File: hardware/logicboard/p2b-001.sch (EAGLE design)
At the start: 54 parts, among them IC1 74LS06N, IC2 4066N, J1 MKR, J2 GPIO, J3 Vcc, J4 RLY, J5 SPI, J7 DIN5, J8 DIN5, J9 DIN5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

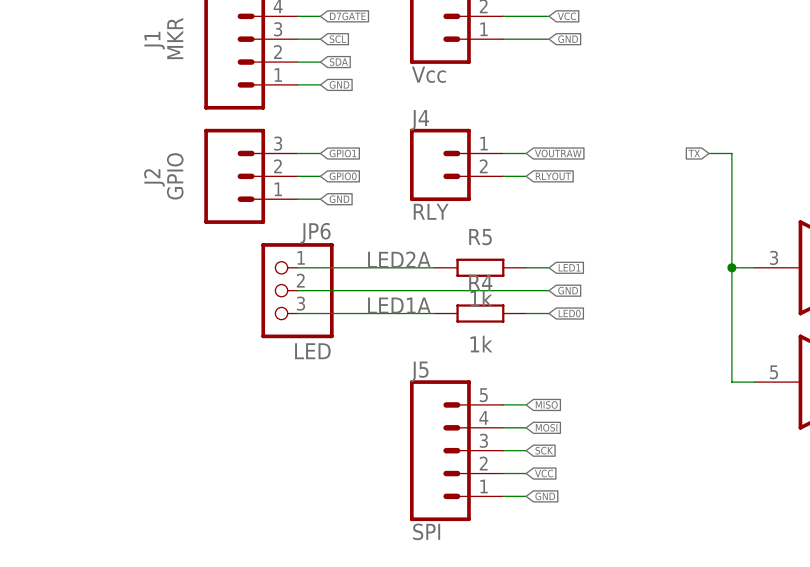
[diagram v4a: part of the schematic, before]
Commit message: Added silk of LED0/1.
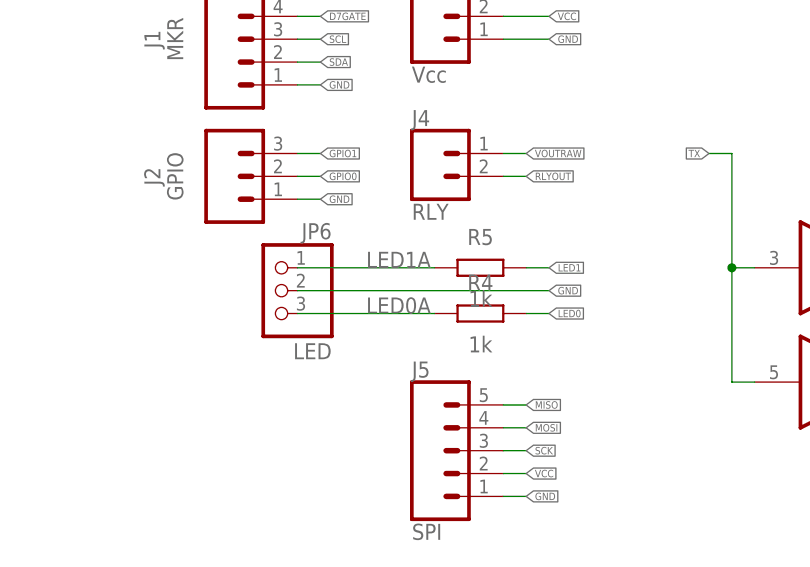
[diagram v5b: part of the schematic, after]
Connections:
- removed net LED2A: JP6.1, R5.1
- new net LED0A: JP6.3, R4.1
- net LED1A: now also JP6.1, R5.1; no longer JP6.3, R4.1
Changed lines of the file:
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@@
 </segment>
 </net>
-<net name="LED2A" class="0">
+<net name="LED1A" class="0">
 <segment>
 <wire x1="88.9" y1="38.1" x2="73.66" y2="38.1" width="0.1524" layer="91"/>
@@
 </segment>
 </net>
-<net name="LED1A" class="0">
+<net name="LED0A" class="0">
 <segment>
 <wire x1="88.9" y1="33.02" x2="73.66" y2="33.02" width="0.1524" layer="91"/>

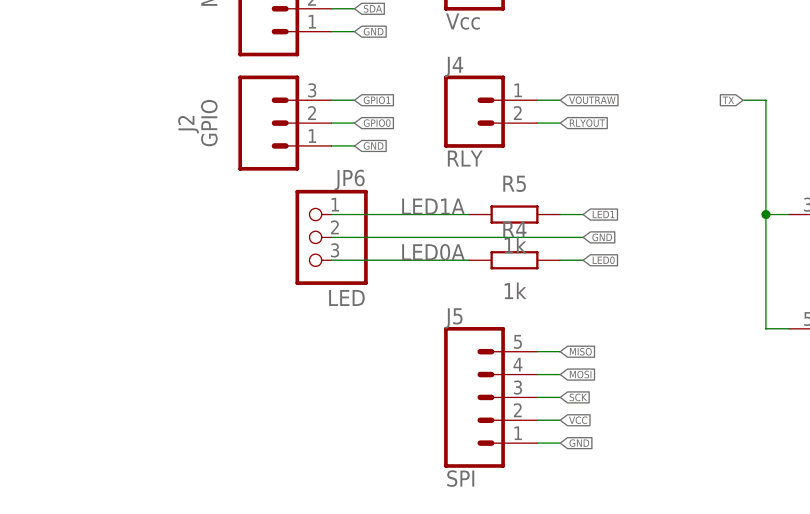
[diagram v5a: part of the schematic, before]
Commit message: Added J6 (LED connector).
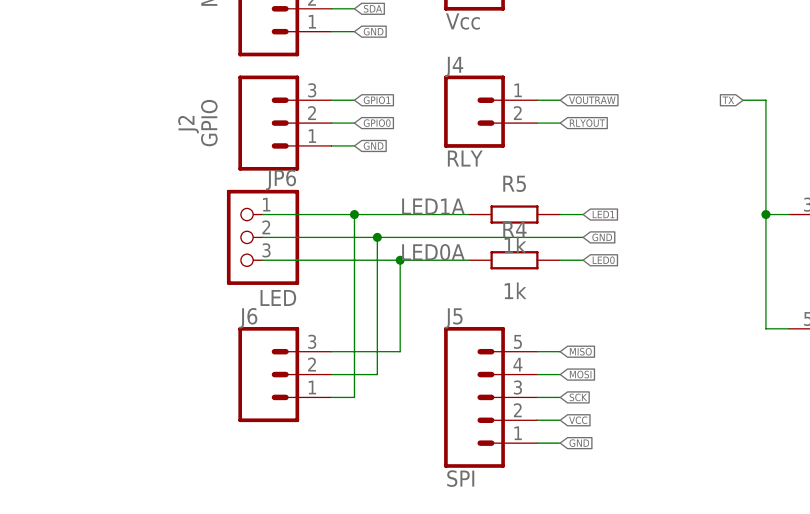
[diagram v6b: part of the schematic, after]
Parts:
- added J6: (no value), SparkFun-Connectors:CONN_03JST-PTH-VERT
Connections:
- net GND: now also J6.2
- net LED0A: now also J6.3
- net LED1A: now also J6.1
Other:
- moved on the sheet: JP6
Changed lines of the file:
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@@
 <part name="P+5" library="supply1" library_urn="urn:adsk.eagle:library:371" deviceset="VCC" device=""/>
 <part name="SV3" library="con-ml" library_urn="urn:adsk.eagle:library:164" deviceset="ML14E" device="" package3d_urn="urn:adsk.eagle:package:8693/1"/>
+<part name="J6" library="SparkFun-Connectors" library_urn="urn:adsk.eagle:library:513" deviceset="CONN_03" device="JST-PTH-VERT" package3d_urn="urn:adsk.eagle:package:38080/1"/>
 </parts>
 <sheets>
@@
 <attribute name="VALUE" x="93.98" y="35.56" size="1.778" layer="96" align="top-center"/>
 </instance>
-<instance part="JP6" gate="A" x="71.12" y="35.56" smashed="yes" rot="MR0">
-<attribute name="NAME" x="77.47" y="41.275" size="1.778" layer="95" rot="MR0"/>
-<attribute name="VALUE" x="77.47" y="27.94" size="1.778" layer="96" rot="MR0"/>
+<instance part="JP6" gate="A" x="63.5" y="35.56" smashed="yes" rot="MR0">
+<attribute name="NAME" x="69.85" y="41.275" size="1.778" layer="95" rot="MR0"/>
+<attribute name="VALUE" x="69.85" y="27.94" size="1.778" layer="96" rot="MR0"/>
 </instance>
 <instance part="JP5" gate="A" x="30.48" y="233.68" smashed="yes" rot="R180">
@@
 <attribute name="NAME" x="337.82" y="215.138" size="1.778" layer="95"/>
 <attribute name="VALUE" x="335.026" y="212.979" size="1.778" layer="96"/>
+</instance>
+<instance part="J6" gate="J$1" x="66.04" y="20.32" smashed="yes">
+<attribute name="VALUE" x="63.5" y="12.954" size="1.778" layer="96" font="vector"/>
+<attribute name="NAME" x="63.5" y="25.908" size="1.778" layer="95" font="vector"/>
 </instance>
 </instances>
@@
 <segment>
 <label x="101.6" y="35.56" size="0.8128" layer="95" xref="yes"/>
-<wire x1="73.66" y1="35.56" x2="101.6" y2="35.56" width="0.1524" layer="91"/>
+<wire x1="66.04" y1="35.56" x2="78.74" y2="35.56" width="0.1524" layer="91"/>
 <pinref part="JP6" gate="A" pin="2"/>
+<pinref part="J6" gate="J$1" pin="2"/>
+<wire x1="78.74" y1="35.56" x2="101.6" y2="35.56" width="0.1524" layer="91"/>
+<wire x1="73.66" y1="20.32" x2="78.74" y2="20.32" width="0.1524" layer="91"/>
+<wire x1="78.74" y1="20.32" x2="78.74" y2="35.56" width="0.1524" layer="91"/>
+<junction x="78.74" y="35.56"/>
 </segment>
 <segment>
@@
 <net name="LED1A" class="0">
 <segment>
-<wire x1="88.9" y1="38.1" x2="73.66" y2="38.1" width="0.1524" layer="91"/>
+<wire x1="88.9" y1="38.1" x2="76.2" y2="38.1" width="0.1524" layer="91"/>
 <label x="81.28" y="38.1" size="1.778" layer="95"/>
 <pinref part="R5" gate="G$1" pin="1"/>
 <pinref part="JP6" gate="A" pin="1"/>
+<pinref part="J6" gate="J$1" pin="1"/>
+<wire x1="76.2" y1="38.1" x2="66.04" y2="38.1" width="0.1524" layer="91"/>
+<wire x1="73.66" y1="17.78" x2="76.2" y2="17.78" width="0.1524" layer="91"/>
+<wire x1="76.2" y1="17.78" x2="76.2" y2="38.1" width="0.1524" layer="91"/>
+<junction x="76.2" y="38.1"/>
 </segment>
 </net>
@@
 <net name="LED0A" class="0">
 <segment>
-<wire x1="88.9" y1="33.02" x2="73.66" y2="33.02" width="0.1524" layer="91"/>
+<wire x1="88.9" y1="33.02" x2="81.28" y2="33.02" width="0.1524" layer="91"/>
 <label x="81.28" y="33.02" size="1.778" layer="95"/>
 <pinref part="R4" gate="G$1" pin="1"/>
 <pinref part="JP6" gate="A" pin="3"/>
-</segment>
-</net>
+<pinref part="J6" gate="J$1" pin="3"/>
+<wire x1="81.28" y1="33.02" x2="66.04" y2="33.02" width="0.1524" layer="91"/>
+<wire x1="73.66" y1="22.86" x2="81.28" y2="22.86" width="0.1524" layer="91"/>
+<wire x1="81.28" y1="22.86" x2="81.28" y2="33.02" width="0.1524" layer="91"/>
+<junction x="81.28" y="33.02"/>
+</segment>
+</net>

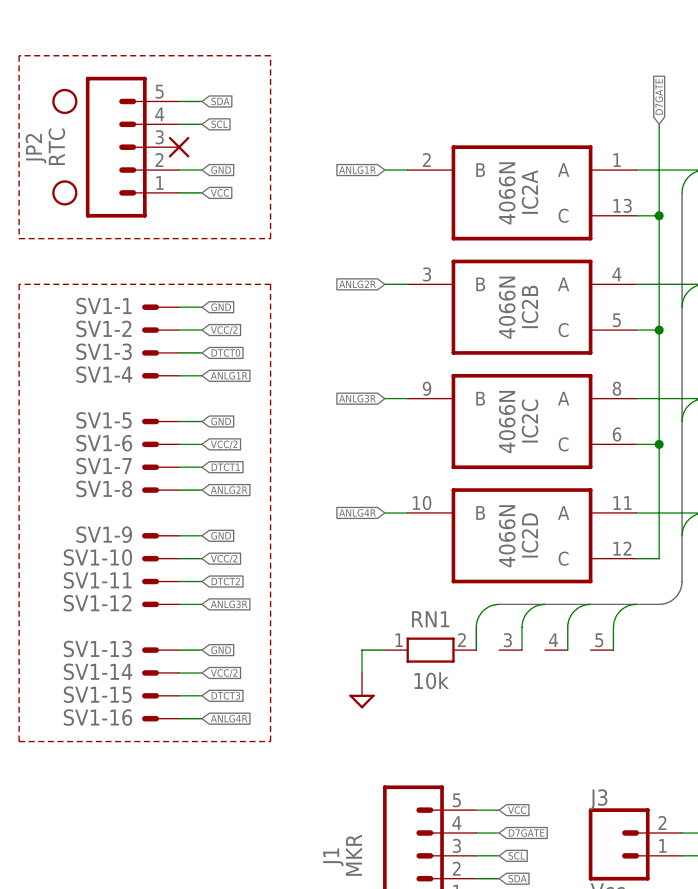
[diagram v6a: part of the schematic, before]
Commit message: Re-arranged GeekPort 2.0.
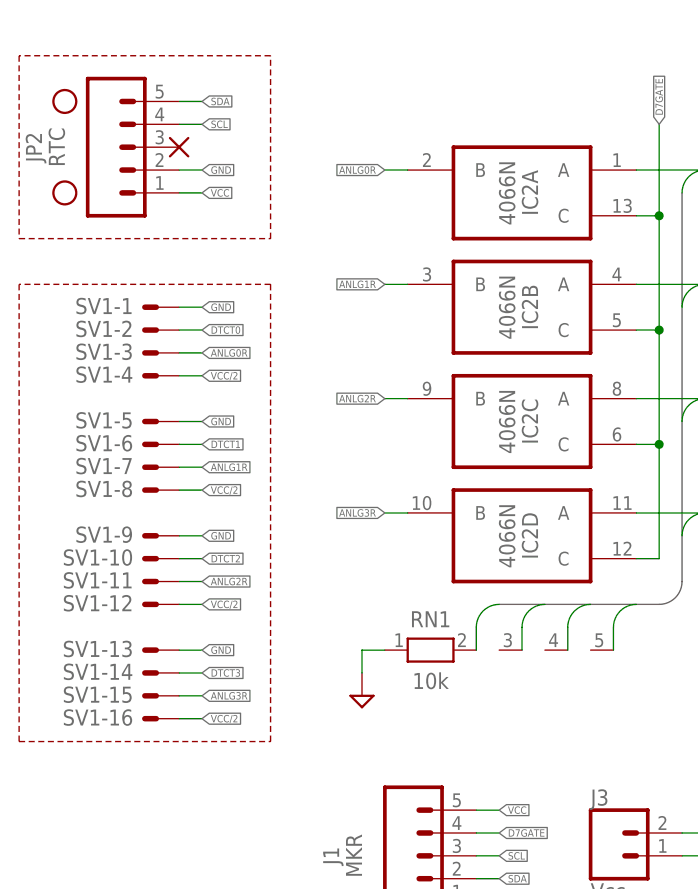
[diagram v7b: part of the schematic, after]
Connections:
- removed net ANLG4R: IC2D.B, SV1-16.S
- new net ANLG0R: IC2A.B, SV1-3.S
- net ANLG1R: now also IC2B.B, SV1-7.S; no longer IC2A.B, SV1-4.S
- net ANLG2R: now also IC2C.B, SV1-11.S; no longer IC2B.B, SV1-8.S
- net ANLG3R: now also IC2D.B, SV1-15.S; no longer IC2C.B, SV1-12.S
- net DTCT0: now also SV1-2.S; no longer SV1-3.S
- net DTCT1: now also SV1-6.S; no longer SV1-7.S
- net DTCT2: now also SV1-10.S; no longer SV1-11.S
- net DTCT3: now also SV1-14.S; no longer SV1-15.S
- net VCC/2: now also SV1-12.S, SV1-16.S, SV1-4.S, SV1-8.S; no longer SV1-10.S, SV1-14.S, SV1-2.S, SV1-6.S
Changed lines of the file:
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@@
-</segment>
-<segment>
-<pinref part="SV1" gate="-3" pin="S"/>
-<wire x1="40.64" y1="119.38" x2="43.18" y2="119.38" width="0.1524" layer="91"/>
-<label x="43.18" y="119.38" size="0.8128" layer="95" xref="yes"/>
 </segment>
 <segment>
@@
 <label x="330.2" y="231.14" size="0.8128" layer="95" rot="R90" xref="yes"/>
 </segment>
+<segment>
+<wire x1="40.64" y1="121.92" x2="43.18" y2="121.92" width="0.1524" layer="91"/>
+<pinref part="SV1" gate="-2" pin="S"/>
+<label x="43.18" y="121.92" size="0.8128" layer="95" xref="yes"/>
+</segment>
 </net>
 <net name="DTCT1" class="0">
@@
 </segment>
 <segment>
-<pinref part="SV1" gate="-7" pin="S"/>
-<wire x1="40.64" y1="106.68" x2="43.18" y2="106.68" width="0.1524" layer="91"/>
-<label x="43.18" y="106.68" size="0.8128" layer="95" xref="yes"/>
-</segment>
-<segment>
 <pinref part="SV3" gate="-12" pin="S"/>
 <wire x1="332.74" y1="226.06" x2="330.2" y2="226.06" width="0.1524" layer="91"/>
 <label x="330.2" y="226.06" size="0.8128" layer="95" rot="R90" xref="yes"/>
 </segment>
+<segment>
+<wire x1="40.64" y1="109.22" x2="43.18" y2="109.22" width="0.1524" layer="91"/>
+<pinref part="SV1" gate="-6" pin="S"/>
+<label x="43.18" y="109.22" size="0.8128" layer="95" xref="yes"/>
+</segment>
 </net>
 <net name="DTCT2" class="0">
@@
 </segment>
 <segment>
-<pinref part="SV1" gate="-11" pin="S"/>
-<wire x1="40.64" y1="93.98" x2="43.18" y2="93.98" width="0.1524" layer="91"/>
-<label x="43.18" y="93.98" size="0.8128" layer="95" xref="yes"/>
-</segment>
-<segment>
 <pinref part="SV3" gate="-13" pin="S"/>
 <wire x1="332.74" y1="220.98" x2="330.2" y2="220.98" width="0.1524" layer="91"/>
 <label x="330.2" y="220.98" size="0.8128" layer="95" rot="R90" xref="yes"/>
 </segment>
+<segment>
+<wire x1="40.64" y1="96.52" x2="43.18" y2="96.52" width="0.1524" layer="91"/>
+<pinref part="SV1" gate="-10" pin="S"/>
+<label x="43.18" y="96.52" size="0.8128" layer="95" xref="yes"/>
+</segment>
 </net>
 <net name="DTCT3" class="0">
@@
 </segment>
 <segment>
-<pinref part="SV1" gate="-15" pin="S"/>
-<wire x1="40.64" y1="81.28" x2="43.18" y2="81.28" width="0.1524" layer="91"/>
-<label x="43.18" y="81.28" size="0.8128" layer="95" xref="yes"/>
-</segment>
-<segment>
 <pinref part="SV3" gate="-14" pin="S"/>
 <wire x1="332.74" y1="215.9" x2="330.2" y2="215.9" width="0.1524" layer="91"/>
 <label x="330.2" y="215.9" size="0.8128" layer="95" rot="R90" xref="yes"/>
+</segment>
+<segment>
+<wire x1="40.64" y1="83.82" x2="43.18" y2="83.82" width="0.1524" layer="91"/>
+<pinref part="SV1" gate="-14" pin="S"/>
+<label x="43.18" y="83.82" size="0.8128" layer="95" xref="yes"/>
 </segment>
 </net>
@@
 </segment>
 <segment>
-<wire x1="40.64" y1="121.92" x2="43.18" y2="121.92" width="0.1524" layer="91"/>
-<pinref part="SV1" gate="-2" pin="S"/>
-<label x="43.18" y="121.92" size="0.8128" layer="95" xref="yes"/>
-</segment>
-<segment>
-<wire x1="40.64" y1="109.22" x2="43.18" y2="109.22" width="0.1524" layer="91"/>
-<pinref part="SV1" gate="-6" pin="S"/>
-<label x="43.18" y="109.22" size="0.8128" layer="95" xref="yes"/>
-</segment>
-<segment>
-<wire x1="40.64" y1="96.52" x2="43.18" y2="96.52" width="0.1524" layer="91"/>
-<pinref part="SV1" gate="-10" pin="S"/>
-<label x="43.18" y="96.52" size="0.8128" layer="95" xref="yes"/>
-</segment>
-<segment>
-<wire x1="40.64" y1="83.82" x2="43.18" y2="83.82" width="0.1524" layer="91"/>
-<pinref part="SV1" gate="-14" pin="S"/>
-<label x="43.18" y="83.82" size="0.8128" layer="95" xref="yes"/>
-</segment>
-<segment>
 <pinref part="P+2" gate="G$1" pin="VCC/2"/>
 <wire x1="66.04" y1="238.76" x2="66.04" y2="231.14" width="0.1524" layer="91"/>
@@
 <wire x1="241.3" y1="119.38" x2="241.3" y2="121.92" width="0.1524" layer="91"/>
 <label x="241.3" y="121.92" size="0.8128" layer="95" rot="R90" xref="yes"/>
+</segment>
+<segment>
+<pinref part="SV1" gate="-4" pin="S"/>
+<wire x1="40.64" y1="116.84" x2="43.18" y2="116.84" width="0.1524" layer="91"/>
+<label x="43.18" y="116.84" size="0.8128" layer="95" xref="yes"/>
+</segment>
+<segment>
+<pinref part="SV1" gate="-8" pin="S"/>
+<wire x1="40.64" y1="104.14" x2="43.18" y2="104.14" width="0.1524" layer="91"/>
+<label x="43.18" y="104.14" size="0.8128" layer="95" xref="yes"/>
+</segment>
+<segment>
+<pinref part="SV1" gate="-12" pin="S"/>
+<wire x1="40.64" y1="91.44" x2="43.18" y2="91.44" width="0.1524" layer="91"/>
+<label x="43.18" y="91.44" size="0.8128" layer="95" xref="yes"/>
+</segment>
+<segment>
+<pinref part="SV1" gate="-16" pin="S"/>
+<wire x1="40.64" y1="78.74" x2="43.18" y2="78.74" width="0.1524" layer="91"/>
+<label x="43.18" y="78.74" size="0.8128" layer="95" xref="yes"/>
 </segment>
 </net>
@@
 </segment>
 </net>
-<net name="ANLG1R" class="3">
-<segment>
-<pinref part="SV1" gate="-4" pin="S"/>
-<wire x1="40.64" y1="116.84" x2="43.18" y2="116.84" width="0.1524" layer="91"/>
-<label x="43.18" y="116.84" size="0.8128" layer="95" xref="yes"/>
-</segment>
+<net name="ANLG0R" class="3">
 <segment>
 <pinref part="IC2" gate="A" pin="B"/>
@@
 <label x="63.5" y="139.7" size="0.8128" layer="95" rot="R180" xref="yes"/>
 </segment>
-</net>
-<net name="ANLG2R" class="3">
-<segment>
-<pinref part="SV1" gate="-8" pin="S"/>
-<wire x1="40.64" y1="104.14" x2="43.18" y2="104.14" width="0.1524" layer="91"/>
-<label x="43.18" y="104.14" size="0.8128" layer="95" xref="yes"/>
-</segment>
+<segment>
+<pinref part="SV1" gate="-3" pin="S"/>
+<wire x1="40.64" y1="119.38" x2="43.18" y2="119.38" width="0.1524" layer="91"/>
+<label x="43.18" y="119.38" size="0.8128" layer="95" xref="yes"/>
+</segment>
+</net>
+<net name="ANLG1R" class="3">
 <segment>
 <pinref part="IC2" gate="B" pin="B"/>
@@
 <label x="63.5" y="127" size="0.8128" layer="95" rot="R180" xref="yes"/>
 </segment>
-</net>
-<net name="ANLG3R" class="3">
-<segment>
-<pinref part="SV1" gate="-12" pin="S"/>
-<wire x1="40.64" y1="91.44" x2="43.18" y2="91.44" width="0.1524" layer="91"/>
-<label x="43.18" y="91.44" size="0.8128" layer="95" xref="yes"/>
-</segment>
+<segment>
+<pinref part="SV1" gate="-7" pin="S"/>
+<wire x1="40.64" y1="106.68" x2="43.18" y2="106.68" width="0.1524" layer="91"/>
+<label x="43.18" y="106.68" size="0.8128" layer="95" xref="yes"/>
+</segment>
+</net>
+<net name="ANLG2R" class="3">
 <segment>
 <pinref part="IC2" gate="C" pin="B"/>
@@
 <label x="63.5" y="114.3" size="0.8128" layer="95" rot="R180" xref="yes"/>
 </segment>
-</net>
-<net name="ANLG4R" class="3">
-<segment>
-<pinref part="SV1" gate="-16" pin="S"/>
-<wire x1="40.64" y1="78.74" x2="43.18" y2="78.74" width="0.1524" layer="91"/>
-<label x="43.18" y="78.74" size="0.8128" layer="95" xref="yes"/>
-</segment>
+<segment>
+<pinref part="SV1" gate="-11" pin="S"/>
+<wire x1="40.64" y1="93.98" x2="43.18" y2="93.98" width="0.1524" layer="91"/>
+<label x="43.18" y="93.98" size="0.8128" layer="95" xref="yes"/>
+</segment>
+</net>
+<net name="ANLG3R" class="3">
 <segment>
 <pinref part="IC2" gate="D" pin="B"/>
@@
 <label x="63.5" y="101.6" size="0.8128" layer="95" rot="R180" xref="yes"/>
 </segment>
-</net>
+<segment>
+<pinref part="SV1" gate="-15" pin="S"/>
+<wire x1="40.64" y1="81.28" x2="43.18" y2="81.28" width="0.1524" layer="91"/>
+<label x="43.18" y="81.28" size="0.8128" layer="95" xref="yes"/>
+</segment>
+</net>

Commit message: Fixed silk.
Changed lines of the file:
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@@
 <part name="X8" library="wirepad" library_urn="urn:adsk.eagle:library:412" deviceset="PAD-N" device=""/>
 <part name="RN3" library="resistor-net" library_urn="urn:adsk.eagle:library:343" deviceset="RN04" device="" package3d_urn="urn:adsk.eagle:package:24976/1" value="4.7k"/>
-<part name="X101" library="wirepad" library_urn="urn:adsk.eagle:library:412" deviceset="PAD-N" device=""/>
 <part name="OK1" library="optocoupler" library_urn="urn:adsk.eagle:library:320" deviceset="HCPL2630" device="" package3d_urn="urn:adsk.eagle:package:21941/1"/>
 <part name="SUPPLY1" library="supply2" deviceset="GND" device=""/>
@@
 <attribute name="VALUE" x="231.14" y="154.94" size="1.778" layer="96" rot="R270" align="top-center"/>
 </instance>
-<instance part="X101" gate="G$1" x="218.44" y="137.16" smashed="yes"/>
 <instance part="OK1" gate="A" x="180.34" y="119.38" smashed="yes" rot="MR0">
 <attribute name="NAME" x="189.865" y="125.095" size="1.778" layer="95" rot="MR0"/>
@@
 </instances>
 <busses>
-<bus name="ANLG[1..4]">
+<bus name="ANLG[0..3]">
 <segment>
 <wire x1="96.52" y1="137.16" x2="96.52" y2="93.98" width="0.762" layer="92"/>
